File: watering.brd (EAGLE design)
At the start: 84.8 x 54.6 mm, 37 parts, among them IC1 LM324N, IC2 7805T, J1 DCJ0202, Q1 IRLZ44Z, T1 2N2222, T2 2N2222, T3 2N2222A

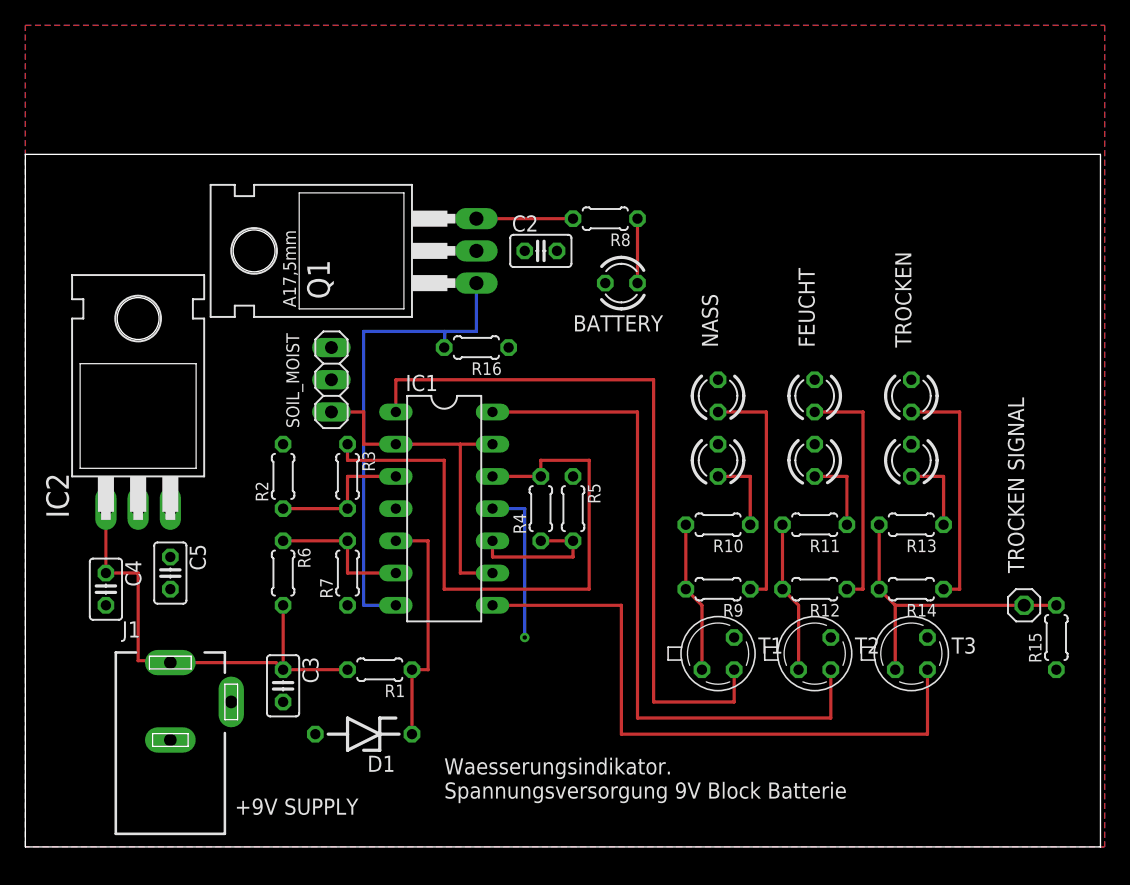
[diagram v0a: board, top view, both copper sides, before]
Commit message: Create watering indicator v2.0 for SMD
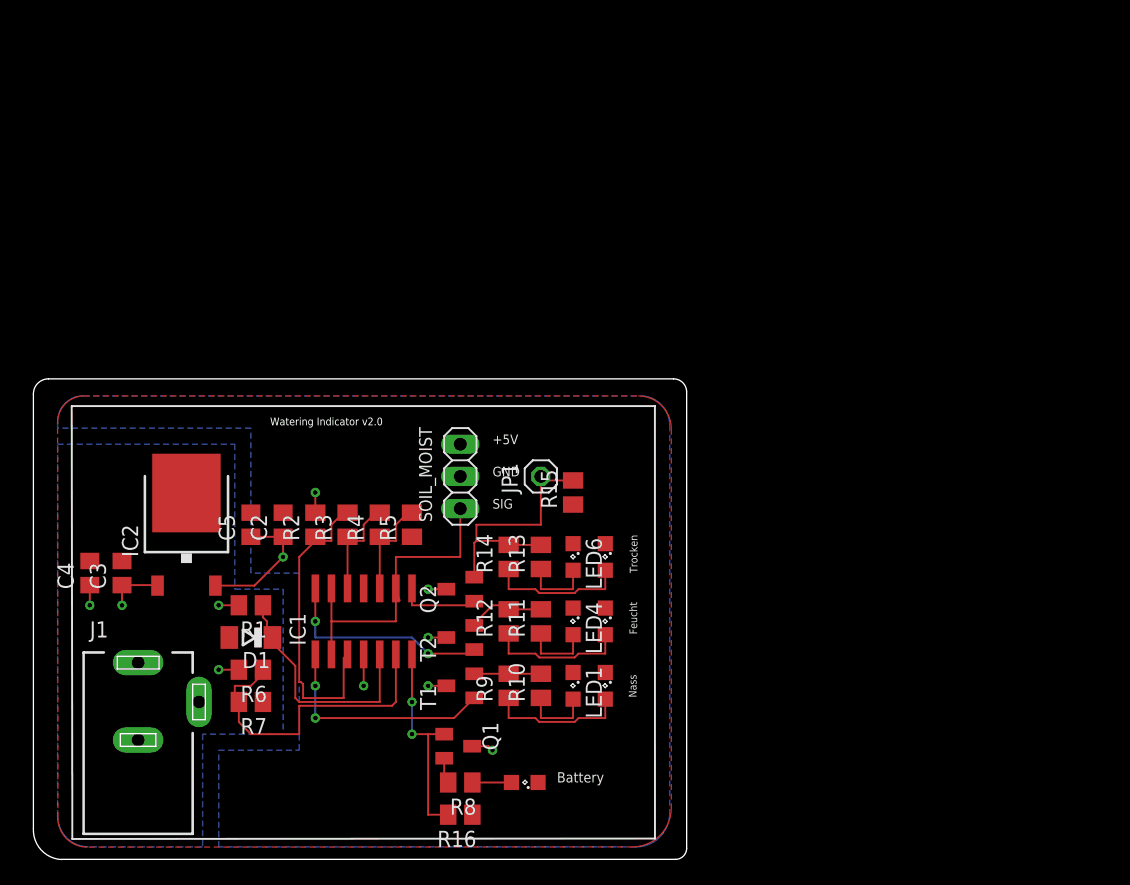
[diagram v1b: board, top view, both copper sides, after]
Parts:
- removed T3: 2N2222A, transistor-npn:TO18
- added Q2: BC848ASMD, transistor-npn:SOT23
- BATTERY, FEUCHT, LED1, LED4, LED6, NASS, TROCKEN: device led:LED3MM -> led:SML0805
- C2, C3, C4, C5: device rcl:C025-025X050 -> rcl:C0805
- D1: device diode:ZDIO-7.5 -> diode:SOD80C
- IC1: value LM324N -> LM324D; device linear:DIL14 -> linear:SO14
- IC2: value 7805T -> 7805DT; device linear:TO220H -> linear:TO252
- Q1: value IRLZ44Z -> BSS123; device transistor-power:TO220BH -> transistor-small-signal:SOT23
- R1, R10, R11, R12, R13, R14, R15, R16, R2, R3, R4, R5, R6, R7, R8, R9: device resistor:0204/5 -> resistor:M0805
- T1, T2: value 2N2222 -> BC848ASMD; device transistor:TO18 -> transistor-npn:SOT23
- moved R8 45.9 mm to (31.8, 5.08)
- moved BATTERY 40.1 mm to (36.8, 5.08)
- moved R15 39.8 mm to (40.6, 27.9)
- moved JP1 39.4 mm to (38.1, 29.2)
- moved Q1 39.4 mm to (31.6, 7.94), turned to 270 degrees
- moved R16 36.9 mm to (31.8, 2.54)
- moved R14 31.9 mm to (35.6, 22.9), turned to 90 degrees
- moved C2 29.6 mm to (17.8, 25.4), turned to 90 degrees
- moved R13 29.3 mm to (38.1, 22.9), turned to 90 degrees
- moved T2 28.0 mm to (31.8, 16.5), turned to 90 degrees
- moved LED6 27.7 mm to (40.6, 22.9), turned to 270 degrees
- moved TROCKEN 27.3 mm to (43.2, 22.9), turned to 270 degrees
- moved NASS 24.5 mm to (43.2, 12.7), turned to 270 degrees
- moved FEUCHT 24.3 mm to (43.2, 17.8), turned to 270 degrees
- moved R12 24.3 mm to (35.6, 17.8), turned to 90 degrees
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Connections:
- net +5V: now also IC2.2, Q1.3, Q2.3; no longer IC2.3, Q1.D, T3.3
- net GND: now also BATTERY.C, FEUCHT.C, IC2.3, LED1.C, LED4.C, LED6.C, NASS.C, TROCKEN.C; no longer BATTERY.K, FEUCHT.K, IC2.2, LED1.K, LED4.K, LED6.K, NASS.K, TROCKEN.K
- net N$14: now also T1.2; no longer T1.1
- net N$15: now also T2.2; no longer T2.1
- net N$18: now also Q2.2; no longer T3.1
- net N$2: now also T1.1; no longer T1.2
- net N$4: now also T2.1; no longer T2.2
- net N$5: now also Q2.1; no longer T3.2
- net N$7: now also Q1.1; no longer Q1.G
- net N$8: now also Q1.2; no longer Q1.S
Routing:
- net N$5: track 49.5 -> 6.37 mm
- net N$11: track 49.5 -> 8.36 mm
- net N$2: track 57.1 -> 18.2 mm, vias 0 -> 2
- net N$4: track 54.6 -> 17.1 mm, vias 0 -> 2
- net +9V: track 36.4 -> 9.18 mm, vias 0 -> 4
- net N$7: track 38.1 -> 16.8 mm, vias 0 -> 2
- net +5V: track 0.00 -> 20.5 mm, vias 0 -> 7
- net N$6: track 11.4 -> 24.8 mm
- net N$1: track 11.4 -> 24.5 mm
- net GND: track 12.7 -> 0.00 mm, vias 1 -> 0
- net N$23: track 19.1 -> 11.0 mm
- net N$21: track 19.1 -> 11.0 mm
- net N$13: track 19.1 -> 11.0 mm
- net N$14: track 12.0 -> 5.25 mm
- net N$15: track 12.0 -> 6.13 mm
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- added copper zone on layer 16, net +9V
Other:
- board size 84.8 x 54.6 mm -> 51.5 x 37.9 mm
- board text added: "+5V"
- board text added: "Battery"
- board text added: "Feucht"
- board text added: "GND"
- board text added: "Nass"
- board text added: "SIG"
- board text added: "Trocken"
- board text added: "Watering Indicator v2.0"
- board text removed: "+9V SUPPLY"
- board text removed: "BATTERY"
- board text removed: "FEUCHT"
- board text removed: "NASS"
- board text removed: "SOIL_MOIST"
- board text removed: "TROCKEN"
- board text removed: "TROCKEN SIGNAL"
- board text removed: "Waesserungsindikator. Spannungsversorgung 9V Block Batterie"

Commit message: Update smd version
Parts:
- removed C2: 0.1uF, rcl:C0805
- removed SOIL_MOIST: (no value), pinhead:1X03
- added C1: 0.1uF, rcl:C0805
- added DRILEGEND: (no value), drilegend:DRILEGEND
- added R17, R18: 4.7k, resistor:M0805
- JP1: device pinhead:1X01 -> jumper:JP3Q
- moved R15 18.4 mm to (22.5, 31.1)
- moved JP1 9.09 mm to (29.2, 31.1), turned to 180 degrees
- renumbered IC2 to REG1, Q1 to MOS1, Q2 to T3
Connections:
- removed net N$14: R10.2, R9.2, T1.2
- removed net N$15: R11.2, R12.2, T2.2
- removed net N$18: JP1.1, R13.2, R14.2, R15.2, T3.2
- new net FEUCHT: JP1.3, R11.2, R12.2, R17.2, T2.2
- new net NASS: JP1.1, R10.2, R18.2, R9.2, T1.2
- new net TROCKEN: JP1.5, R13.2, R14.2, R15.2, T3.2
- net +5V: now also C1.2, IC1.3, JP1.4; no longer C2.1, SOIL_MOIST.1
- net GND: now also C1.1, JP1.6, R17.1, R18.1; no longer C2.2, SOIL_MOIST.2
- net N$1: no longer IC1.3
- net SOIL_IN: now also JP1.2; no longer SOIL_MOIST.3
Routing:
- net FEUCHT: track 0.00 -> 34.4 mm, vias 0 -> 1
- net NASS: track 0.00 -> 28.4 mm, vias 0 -> 1
- net TROCKEN: track 0.00 -> 26.4 mm, vias 0 -> 1
- net N$18: track 20.9 -> 0.00 mm
- net N$1: track 24.5 -> 4.66 mm
- net N$15: track 6.13 -> 0.00 mm
- net +5V: track 20.5 -> 26.3 mm
- net N$14: track 5.25 -> 0.00 mm
- net SOIL_IN: track 25.3 -> 28.4 mm
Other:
- board text added: "LED2"
- board text added: "LED3"
- board text added: "LED5"
- board text added: "MOSFET Pull-Down"
- board text removed: "+5V"
- board text removed: "GND"
- board text removed: "SIG"

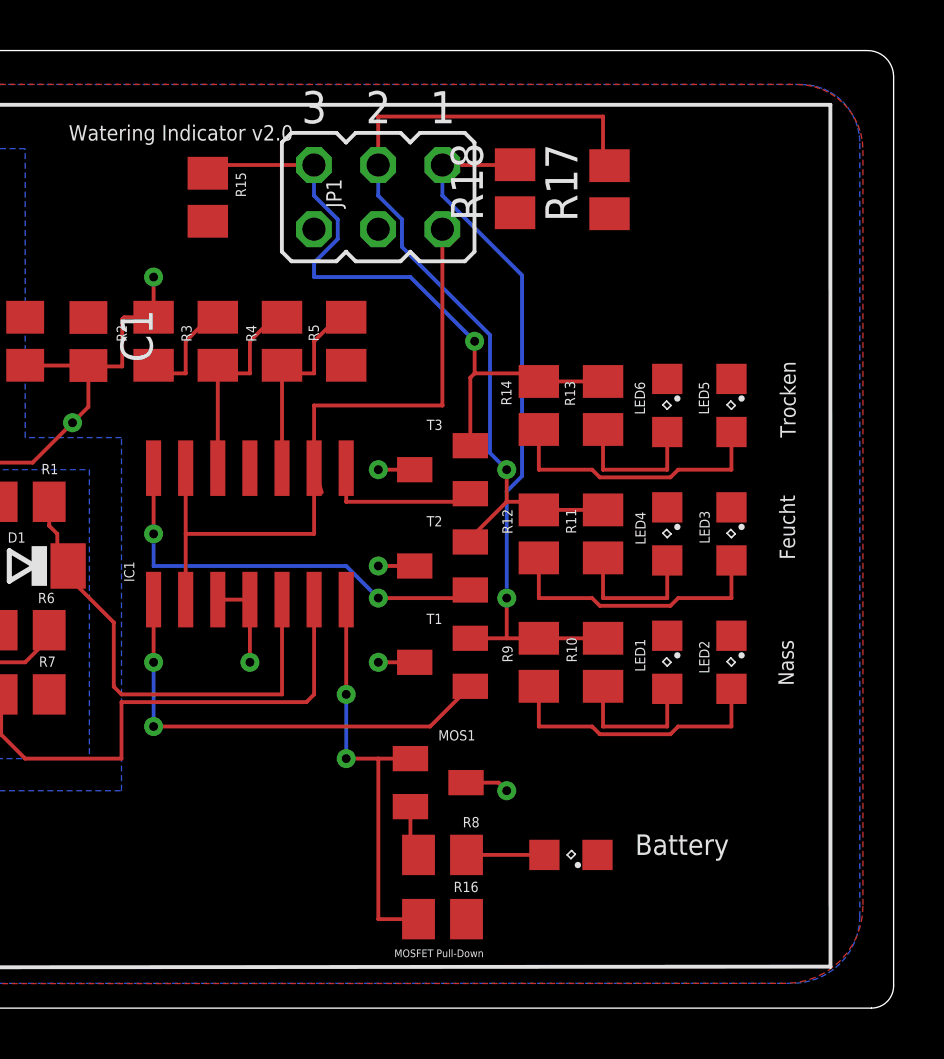
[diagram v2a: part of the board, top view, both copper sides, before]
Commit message: Replace BJT to MOSFET for led switching
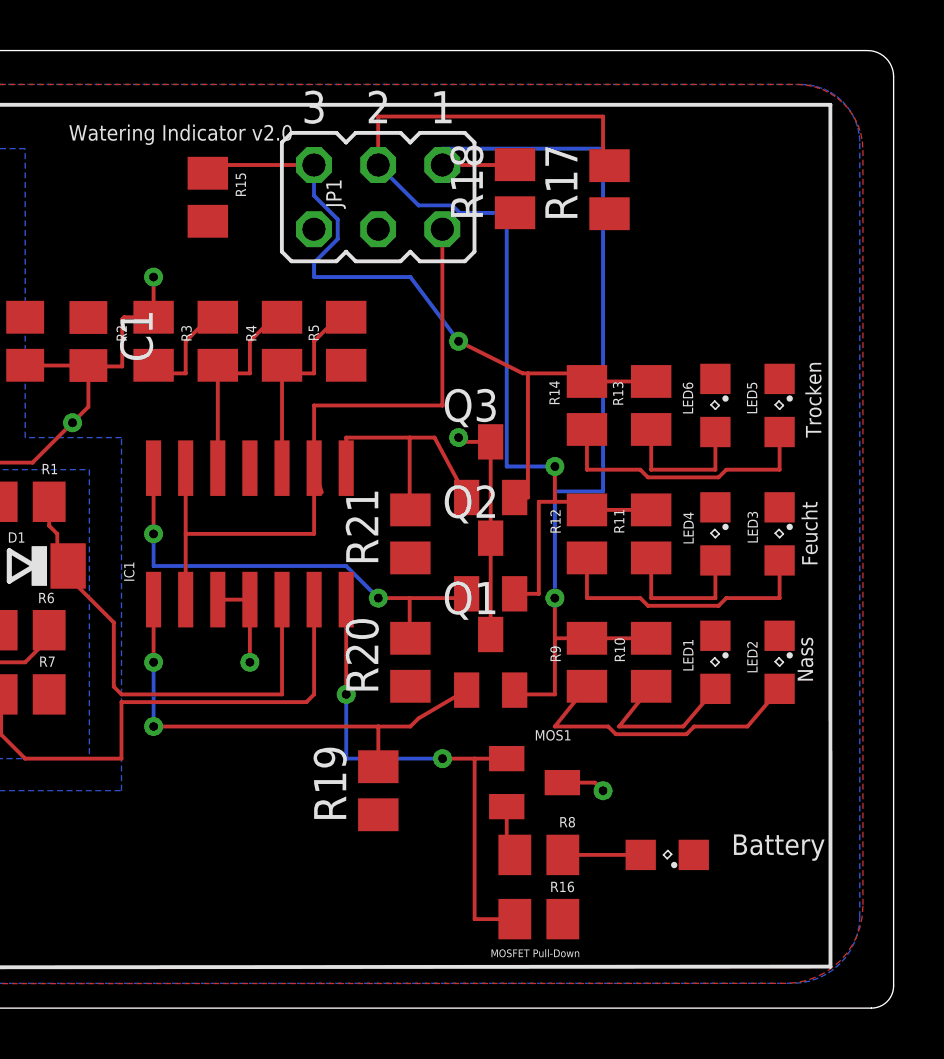
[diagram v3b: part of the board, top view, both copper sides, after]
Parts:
- removed T1, T2, T3: BC848ASMD, transistor-npn:SOT23
- added Q1, Q2, Q3: BSS123, transistor-small-signal:SOT23
- added R19, R20, R21: 10k, resistor:M0805
- moved BATTERY 3.81 mm to (40.6, 5.08)
- moved MOS1 3.81 mm to (35.4, 7.94)
- moved R16 3.81 mm to (35.6, 2.54)
- moved R8 3.81 mm to (35.6, 5.08)
- moved FEUCHT 1.91 mm to (45.1, 17.8)
- moved LED1 1.91 mm to (42.5, 12.7)
- moved LED4 1.91 mm to (42.5, 17.8)
- moved LED6 1.91 mm to (42.5, 22.9)
- moved NASS 1.91 mm to (45.1, 12.7)
- moved R10 1.91 mm to (40.0, 12.7)
- moved R11 1.91 mm to (40.0, 17.8)
- moved R12 1.91 mm to (37.5, 17.8)
- moved R13 1.91 mm to (40.0, 22.9)
- moved R14 1.91 mm to (37.5, 22.9)
- moved R9 1.91 mm to (37.5, 12.7)
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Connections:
- net +5V: now also Q1.3, Q2.3, Q3.3; no longer T1.3, T2.3, T3.3
- net FEUCHT: now also Q2.2; no longer T2.2
- net GND: now also R19.1, R20.1, R21.1
- net N$2: now also Q1.1, R19.2; no longer T1.1
- net N$4: now also Q2.1, R20.2; no longer T2.1
- net N$5: now also Q3.1, R21.2; no longer T3.1
- net NASS: now also Q1.2; no longer T1.2
- net TROCKEN: now also Q3.2; no longer T3.2
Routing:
- net NASS: track 28.4 -> 38.9 mm
- net FEUCHT: track 34.4 -> 41.4 mm
- net +5V: track 26.3 -> 31.0 mm, vias 7 -> 5
- net N$5: track 6.37 -> 10.3 mm
- net N$7: track 16.8 -> 20.6 mm
- net TROCKEN: track 26.4 -> 30.0 mm
- net N$4: track 17.1 -> 18.5 mm
- net N$2: track 18.2 -> 19.4 mm
- net N$13: track 11.0 -> 11.9 mm
- net N$10: track 5.62 -> 6.53 mm

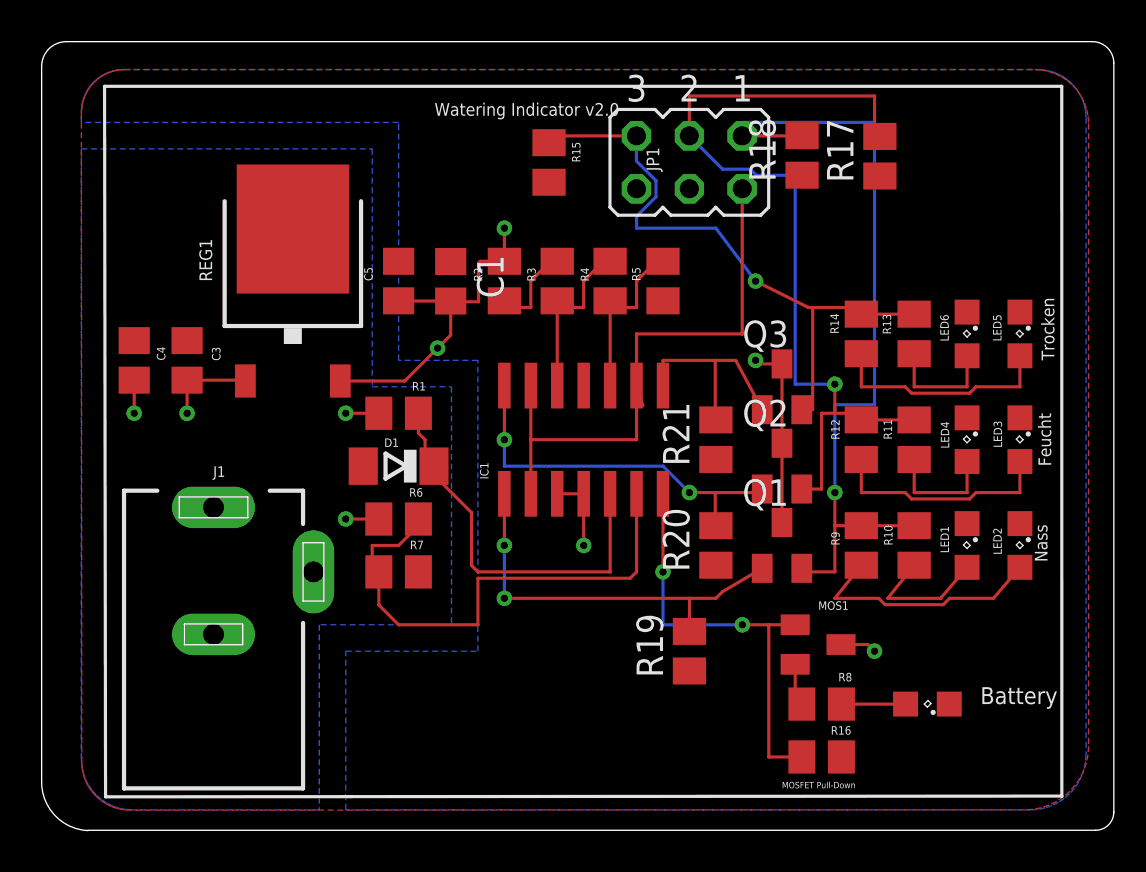
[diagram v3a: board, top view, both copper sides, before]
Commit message: Change zener diode package
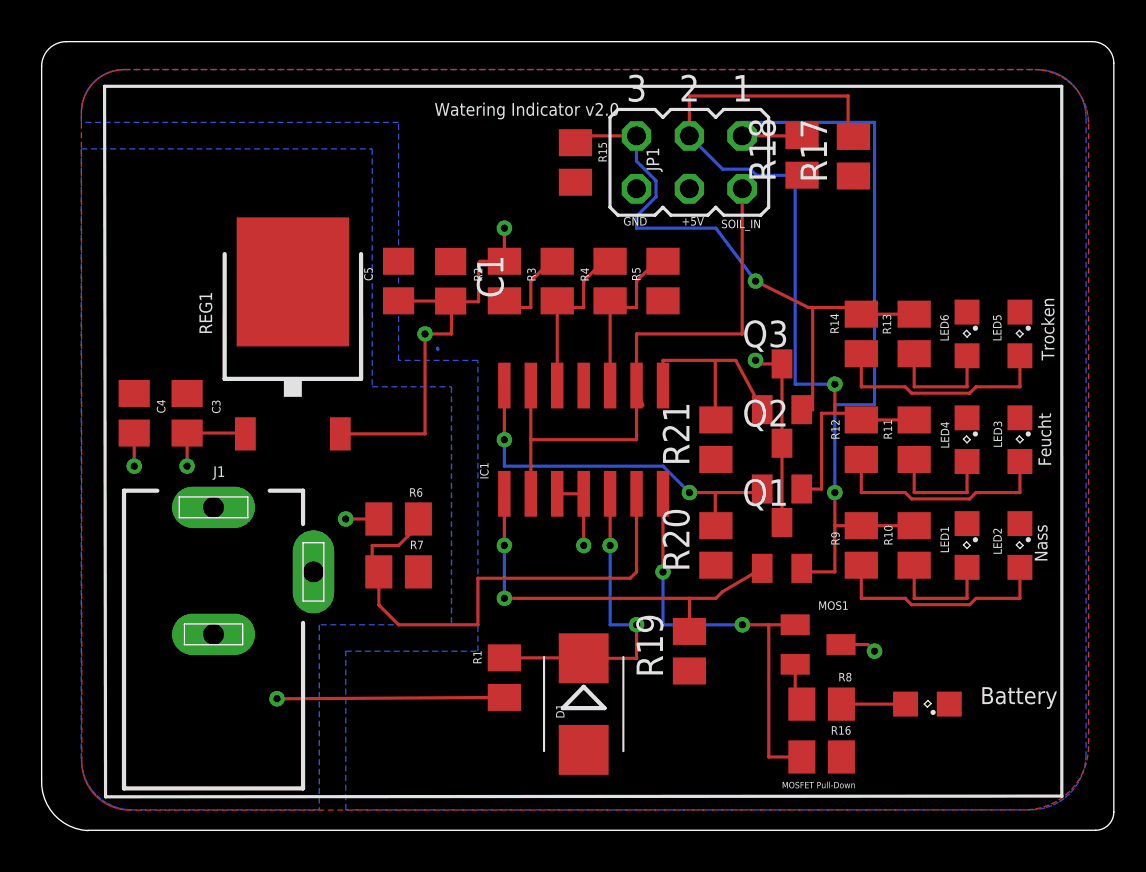
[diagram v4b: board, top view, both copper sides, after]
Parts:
- D1: device diode:SOD80C -> diode:SMB
- moved D1 14.5 mm to (24.1, 5.08), turned to 270 degrees
- moved R1 13.7 mm to (20.3, 6.35), turned to 270 degrees
- moved C3 2.54 mm to (5.08, 19.1)
- moved C4 2.54 mm to (2.54, 19.1)
- moved REG1 2.54 mm to (10.2, 22.9)
- moved R15 1.27 mm to (23.7, 31.1)
- moved R17 1.27 mm to (37.1, 31.4)
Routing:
- net +9V: track 9.18 -> 18.5 mm
- net +5V: track 31.0 -> 34.9 mm
- net N$3: track 18.9 -> 15.5 mm, vias 0 -> 2
- net TROCKEN: track 30.0 -> 28.7 mm
- net FEUCHT: track 41.4 -> 40.2 mm
- net N$13: track 11.9 -> 11.0 mm
- net N$10: track 6.53 -> 5.62 mm
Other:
- board text added: "+5V"
- board text added: "GND"
- board text added: "SOIL_IN"
